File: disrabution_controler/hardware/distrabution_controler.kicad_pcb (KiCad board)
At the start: 4 copper layers, 246 x 110 mm, 266 parts, among them J1 Conn_Coaxial, J3 JTAG, J5 PROG_PORT, Q1 NMOS, Q10 PMOS, Q11 PMOS, Q12 PMOS, Q13 PMOS, Q14 PMOS, Q15 PMOS, Q16 PMOS, Q17 PMOS, Q18 PMOS, Q19 PMOS, Q2 NMOS, Q20 PMOS, Q3 NMOS, Q4 PMOS, Q5 PMOS, Q6 PMOS, Q7 PMOS, Q8 PMOS, Q9 PMOS, U1 TJA1043T/1J, U2 ESP32-S2FH2, U3 PI4IOE5V6416LEX, U4 ECMF02-2AMX6, U5 ADS7128, U6 ADS7128, U7 AP62150WU, Y1 40 MHz

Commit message: more hardware work on disrabution controler nearing ifc
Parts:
- added H20: MountingHole, MountingHole:MountingHole_4.3mm_M4, F.Cu at (49.4, 89.5)
- added H21: MountingHole, MountingHole:MountingHole_4.3mm_M4, F.Cu at (49.2, 124.5)
- added H22: MountingHole, MountingHole:MountingHole_4.3mm_M4, F.Cu at (189.3, 95.7)
- added H23: MountingHole, MountingHole:MountingHole_4.3mm_M4, F.Cu at (196.3, 129.1)
- added H24: MountingHole, MountingHole:MountingHole_4.3mm_M4, F.Cu at (250.1, 160.2)
- C1, C12, C13, C14, C15, C16, C17, C2, C3, C4, C5, C6, D20, D21, JP1, R1, R2, R21, R22, R32, R33: moved to B.Cu
- J2, U4: moved to F.Cu
- L1: footprint Resistor_SMD:R_0603_1608Metric -> Inductor_SMD:L_Bourns_SDR0604
- Q1, Q2, Q3: footprint Resistor_SMD:R_0603_1608Metric -> Package_TO_SOT_SMD:SOT-23
- moved TP25 314.0 mm to (210.8, 78.4)
- moved L1 312.4 mm to (208.8, 83.4), turned to 90 degrees
- moved TP29 311.3 mm to (207.0, 91.0), turned to 180 degrees
- moved C34 309.9 mm to (212.9, 87.2), turned to -90 degrees
- moved Q2 305.6 mm to (202.0, 89.3), turned to 180 degrees
- moved TP26 305.4 mm to (209.0, 91.0), turned to 180 degrees
- moved Q3 304.9 mm to (202.0, 92.7), turned to 180 degrees
- moved R53 303.5 mm to (207.5, 88.0), turned to 180 degrees
- moved C32 303.0 mm to (202.7, 83.0)
- moved TP2 302.7 mm to (248.3, 94.0)
- moved TP1 302.1 mm to (248.3, 91.9)
- moved R51 301.4 mm to (210.5, 88.0), turned to 180 degrees
- moved TP28 301.3 mm to (196.0, 92.2)
- moved C33 301.0 mm to (199.2, 85.5), turned to 90 degrees
- moved TP27 300.6 mm to (196.0, 90.1), turned to 90 degrees
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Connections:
- net Net-(J1-In) renamed LNA
- D20 pad 5: ESP_RX -> GPIO12
- D20 pad 6: unconnected-(D20-K5-Pad6) -> ESP_RX
- D20 pad 7: GPIO12 -> RST
- D20 pad 8: unconnected-(D20-K7-Pad8) -> ESP_IO0
- D21 pad 1: GPIO11 -> GPIO6
- D21 pad 2: GPIO10 -> GPIO8
- D21 pad 4: GPIO9 -> GPIO11
- D21 pad 5: GPIO8 -> DAC_2
- D21 pad 6: GPIO7 -> DAC_1
- D21 pad 7: GPIO6 -> GPIO10
- D21 pad 8: DAC_2 -> GPIO9
- D21 pad 9: DAC_1 -> GPIO7
- Q1 pad 1: CAR_ACC -> /MCU_IO/CAR_ACC_ESD
- Q1 pad 2: /MCU_IO/CAR_ACC_ESD -> GND
- Q2 pad 1: Net-(Q2-D) -> Net-(Q2-G)
- Q2 pad 2: Net-(Q2-G) -> GND
- Q3 pad 1: Net-(Q2-G) -> ALLOW_Q_DRAW
- Q3 pad 2: ALLOW_Q_DRAW -> GND
- U2 pad 37: CAN_WAKE -> CAN_ERR
- U2 pad 38: CAN_ERR -> CAN_WAKE
- U2 pad 40: CAN_EN -> CAN_TX
- U2 pad 42: CAN_TX -> CAN_EN
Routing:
- net +3V3: track 27.7 -> 679.7 mm, vias 4 -> 40
- net I2C_SDA: track 0.00 -> 327.9 mm, vias 0 -> 7
- net I2C_SCL: track 0.00 -> 327.2 mm, vias 0 -> 6
- net Net-(D16-DIN): track 0.00 -> 288.3 mm, vias 0 -> 2
- net RST: track 0.00 -> 245.0 mm, vias 0 -> 3
- net DISRABUTION_NEO_PIXELS: track 0.00 -> 232.2 mm, vias 0 -> 2
- net CAR_ACC: track 0.00 -> 198.8 mm
- net IOX0_INT: track 6.40 -> 181.3 mm, vias 0 -> 3
- net ADC_02_ALERT: track 0.00 -> 160.0 mm, vias 0 -> 4
- net ADC_01_ALERT: track 0.00 -> 134.2 mm, vias 0 -> 4
- net GPIO12: track 0.00 -> 124.1 mm, vias 0 -> 1
- net GPIO6: track 0.00 -> 103.9 mm
- net GPIO7: track 0.00 -> 96.2 mm
- net DAC_1: track 0.00 -> 92.4 mm, vias 0 -> 2
- net ESP_RX: track 0.00 -> 89.1 mm, vias 0 -> 1
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- added copper zone on B.Cu, net +3V3
- added copper zone on F.Cu, net +3V3
- added copper zone on F.Cu, net GND
- added copper zone on In2.Cu, net GND
- added copper zone on F.Cu, net Net-(U7-BST)
- added copper zone on In2.Cu, net PERIPHERAL_PWR
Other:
- board text added: "+3V3"
- board text added: "CAR POWER SYSTEM DISRABUTION CONTROLER REV A TOKYO ANDREANA GPL-3.0 FLA PER CHANEL SHAL NOT EXCEED 30A"
- board text added: "CHANEL 1"
- board text added: "CHANEL 10"
- board text added: "CHANEL 11"
- board text added: "CHANEL 12"
- board text added: "CHANEL 13"
- board text added: "CHANEL 14"
- board text added: "CHANEL 15"
- board text added: "CHANEL 16"
- board text added: "CHANEL 2"
- board text added: "CHANEL 3"
- board text added: "CHANEL 4"
- board text added: "CHANEL 5"
- board text added: "CHANEL 6"
- board text added: "CHANEL 7"
- board text added: "CHANEL 8"
- board text added: "CHANEL 9"
- board text added: "GND"
- board text added: "IO0"
- board text added: "JTAG"
- board text added: "MDT0"
- board text added: "MTCK"
- board text added: "MTDI"
- board text added: "MTMS"
- board text added: "PROG"
- board text added: "RST"
- board text added: "RX"
- board text added: "TX"
- board text added: "WI-FI"

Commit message: fixed haredware issue
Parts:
- added Q21: NMOS, Package_TO_SOT_SMD:SOT-23, F.Cu at (27.0, 132.0)
- added Q22: NMOS, Package_TO_SOT_SMD:SOT-23, F.Cu at (49.0, 132.0)
- added Q23: NMOS, Package_TO_SOT_SMD:SOT-23, F.Cu at (71.0, 132.0)
- added Q24: NMOS, Package_TO_SOT_SMD:SOT-23, F.Cu at (167.2, 113.5)
- added Q25: NMOS, Package_TO_SOT_SMD:SOT-23, F.Cu at (93.0, 132.0)
- added Q26: NMOS, Package_TO_SOT_SMD:SOT-23, F.Cu at (115.0, 132.0)
- added Q27: NMOS, Package_TO_SOT_SMD:SOT-23, F.Cu at (137.0, 132.0)
- added Q28: NMOS, Package_TO_SOT_SMD:SOT-23, F.Cu at (159.0, 132.0)
- added Q29: NMOS, Package_TO_SOT_SMD:SOT-23, F.Cu at (181.0, 132.0)
- added Q30: NMOS, Package_TO_SOT_SMD:SOT-23, F.Cu at (188.7, 86.0)
- added Q31: NMOS, Package_TO_SOT_SMD:SOT-23, F.Cu at (166.9, 86.0)
- added Q32: NMOS, Package_TO_SOT_SMD:SOT-23, F.Cu at (144.7, 86.0)
- added Q33: NMOS, Package_TO_SOT_SMD:SOT-23, F.Cu at (122.8, 86.0)
- added Q34: NMOS, Package_TO_SOT_SMD:SOT-23, F.Cu at (100.7, 86.0)
- added Q35: NMOS, Package_TO_SOT_SMD:SOT-23, F.Cu at (78.8, 86.0)
- added Q36: NMOS, Package_TO_SOT_SMD:SOT-23, F.Cu at (56.9, 86.0)
- added Q37: NMOS, Package_TO_SOT_SMD:SOT-23, F.Cu at (34.8, 86.0)
- added TP48: ~, TestPoint:TestPoint_Pad_D1.0mm, F.Cu at (24.0, 129.7)
- added TP49: ~, TestPoint:TestPoint_Pad_D1.0mm, F.Cu at (46.0, 129.7)
- added TP50: ~, TestPoint:TestPoint_Pad_D1.0mm, F.Cu at (68.0, 129.7)
- added TP51: ~, TestPoint:TestPoint_Pad_D1.0mm, F.Cu at (90.0, 129.7)
- added TP52: ~, TestPoint:TestPoint_Pad_D1.0mm, F.Cu at (112.0, 129.7)
- added TP53: ~, TestPoint:TestPoint_Pad_D1.0mm, F.Cu at (134.0, 129.7)
- added TP54: ~, TestPoint:TestPoint_Pad_D1.0mm, F.Cu at (156.0, 129.7)
- added TP55: ~, TestPoint:TestPoint_Pad_D1.0mm, F.Cu at (178.0, 129.7)
- added TP56: ~, TestPoint:TestPoint_Pad_D1.0mm, F.Cu at (191.3, 88.4)
- added TP57: ~, TestPoint:TestPoint_Pad_D1.0mm, F.Cu at (169.2, 88.6)
- added TP58: ~, TestPoint:TestPoint_Pad_D1.0mm, F.Cu at (147.2, 88.4)
- added TP59: ~, TestPoint:TestPoint_Pad_D1.0mm, F.Cu at (125.4, 88.4)
- added TP60: ~, TestPoint:TestPoint_Pad_D1.0mm, F.Cu at (103.3, 88.4)
- added TP61: ~, TestPoint:TestPoint_Pad_D1.0mm, F.Cu at (81.2, 88.7)
- added TP62: ~, TestPoint:TestPoint_Pad_D1.0mm, F.Cu at (59.4, 88.4)
- added TP63: ~, TestPoint:TestPoint_Pad_D1.0mm, F.Cu at (37.2, 88.5)
- added TP64: ~, TestPoint:TestPoint_Pad_D1.0mm, F.Cu at (168.4, 117.5)
- F1, F10, F11, F12, F13, F14, F15, F16, F17, F2, F3, F4, F5, F6, F7, F8, F9: value Fuse_Small -> ~
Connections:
- net IOX0_INT renamed IOX_0_INT
- Q10 pad 4: CH7_GATE -> Net-(Q10-G)
- Q11 pad 4: CH8_GATE -> Net-(Q11-G)
- Q12 pad 4: CH9_GATE -> Net-(Q12-G)
- Q13 pad 4: CH10_GATE -> Net-(Q13-G)
- Q14 pad 4: CH11_GATE -> Net-(Q14-G)
- Q15 pad 4: CH12_GATE -> Net-(Q15-G)
- Q16 pad 4: CH13_GATE -> Net-(Q16-G)
- Q17 pad 4: CH14_GATE -> Net-(Q17-G)
- Q18 pad 4: CH15_GATE -> Net-(Q18-G)
- Q19 pad 4: CH16_GATE -> Net-(Q19-G)
- Q20 pad 4: PERIPHERAL_PWR_GATE -> Net-(Q20-G)
- Q4 pad 4: CH1_GATE -> Net-(Q21-D)
- Q5 pad 4: CH2_GATE -> Net-(Q22-D)
- Q6 pad 4: CH3_GATE -> Net-(Q23-D)
- Q7 pad 4: CH4_GATE -> Net-(Q25-D)
- Q8 pad 4: CH5_GATE -> Net-(Q26-D)
- Q9 pad 4: CH6_GATE -> Net-(Q27-D)
- R56 pad 2: CH1_GATE -> Net-(Q21-D)
- R57 pad 2: CH2_GATE -> Net-(Q22-D)
- R58 pad 2: CH3_GATE -> Net-(Q23-D)
- R59 pad 2: CH4_GATE -> Net-(Q25-D)
- R60 pad 2: CH5_GATE -> Net-(Q26-D)
- R61 pad 2: CH6_GATE -> Net-(Q27-D)
- R62 pad 2: CH7_GATE -> Net-(Q10-G)
- R63 pad 2: CH8_GATE -> Net-(Q11-G)
- R72 pad 2: CH9_GATE -> Net-(Q12-G)
- R73 pad 2: CH10_GATE -> Net-(Q13-G)
- R74 pad 2: CH11_GATE -> Net-(Q14-G)
- R75 pad 2: CH12_GATE -> Net-(Q15-G)
- R76 pad 2: CH13_GATE -> Net-(Q16-G)
- R77 pad 2: CH14_GATE -> Net-(Q17-G)
- R78 pad 2: CH15_GATE -> Net-(Q18-G)
- R79 pad 2: CH16_GATE -> Net-(Q19-G)
- R88 pad 2: PERIPHERAL_PWR_GATE -> Net-(Q20-G)
- TP30 pad 1: CH1_GATE -> Net-(Q21-D)
- TP31 pad 1: CH2_GATE -> Net-(Q22-D)
- TP32 pad 1: CH3_GATE -> Net-(Q23-D)
- TP33 pad 1: CH4_GATE -> Net-(Q25-D)
- TP34 pad 1: CH5_GATE -> Net-(Q26-D)
- TP35 pad 1: CH6_GATE -> Net-(Q27-D)
- TP36 pad 1: CH7_GATE -> Net-(Q10-G)
- TP37 pad 1: CH8_GATE -> Net-(Q11-G)
- TP38 pad 1: CH9_GATE -> Net-(Q12-G)
- TP39 pad 1: CH10_GATE -> Net-(Q13-G)
- TP40 pad 1: CH11_GATE -> Net-(Q14-G)
- TP41 pad 1: CH12_GATE -> Net-(Q15-G)
- TP42 pad 1: CH13_GATE -> Net-(Q16-G)
- TP43 pad 1: CH14_GATE -> Net-(Q17-G)
- TP44 pad 1: CH15_GATE -> Net-(Q18-G)
- TP45 pad 1: CH16_GATE -> Net-(Q19-G)
- TP47 pad 1: PERIPHERAL_PWR_GATE -> Net-(Q20-G)
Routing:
- net GND: track 128.0 -> 145.9 mm, vias 71 -> 88
- net CH3_GATE: track 44.7 -> 29.5 mm, vias 2 -> 1
- net CH7_GATE: track 130.2 -> 115.1 mm, vias 2 -> 1
- net CH4_GATE: track 65.9 -> 50.9 mm, vias 2 -> 1
- net CH6_GATE: track 108.6 -> 93.7 mm, vias 2 -> 1
- net CH5_GATE: track 87.2 -> 72.3 mm, vias 2 -> 1
- net CH8_GATE: track 151.3 -> 136.5 mm, vias 2 -> 1
- net CH16_GATE: track 37.8 -> 23.4 mm, vias 2 -> 1
- net PERIPHERAL_PWR_GATE: track 75.4 -> 64.1 mm
- net Net-(Q19-G): track 0.00 -> 8.27 mm
- net Net-(Q12-G): track 0.00 -> 7.32 mm
- net Net-(Q20-G): track 0.00 -> 7.21 mm
- net Net-(Q10-G): track 0.00 -> 6.73 mm
- net Net-(Q11-G): track 0.00 -> 6.73 mm
- net Net-(Q22-D): track 0.00 -> 6.73 mm
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
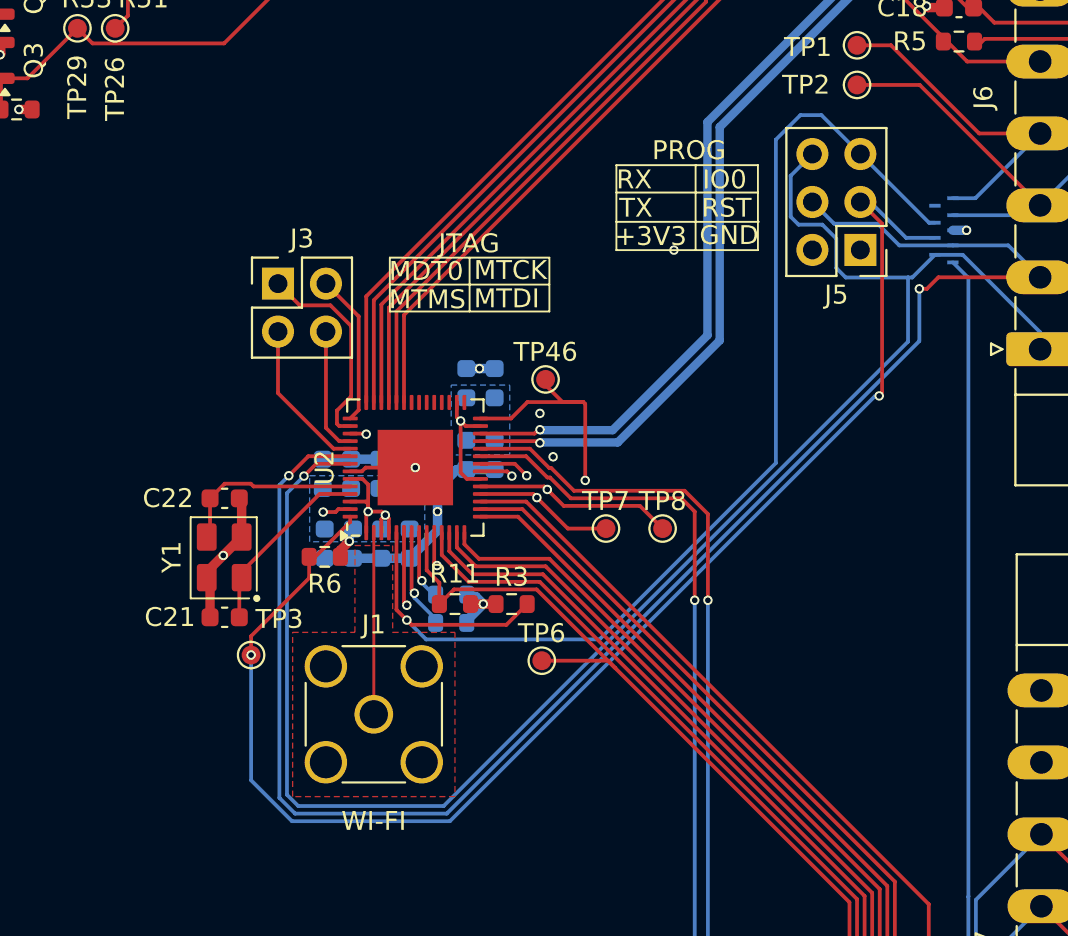
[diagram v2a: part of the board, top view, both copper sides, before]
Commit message: changed programing headder
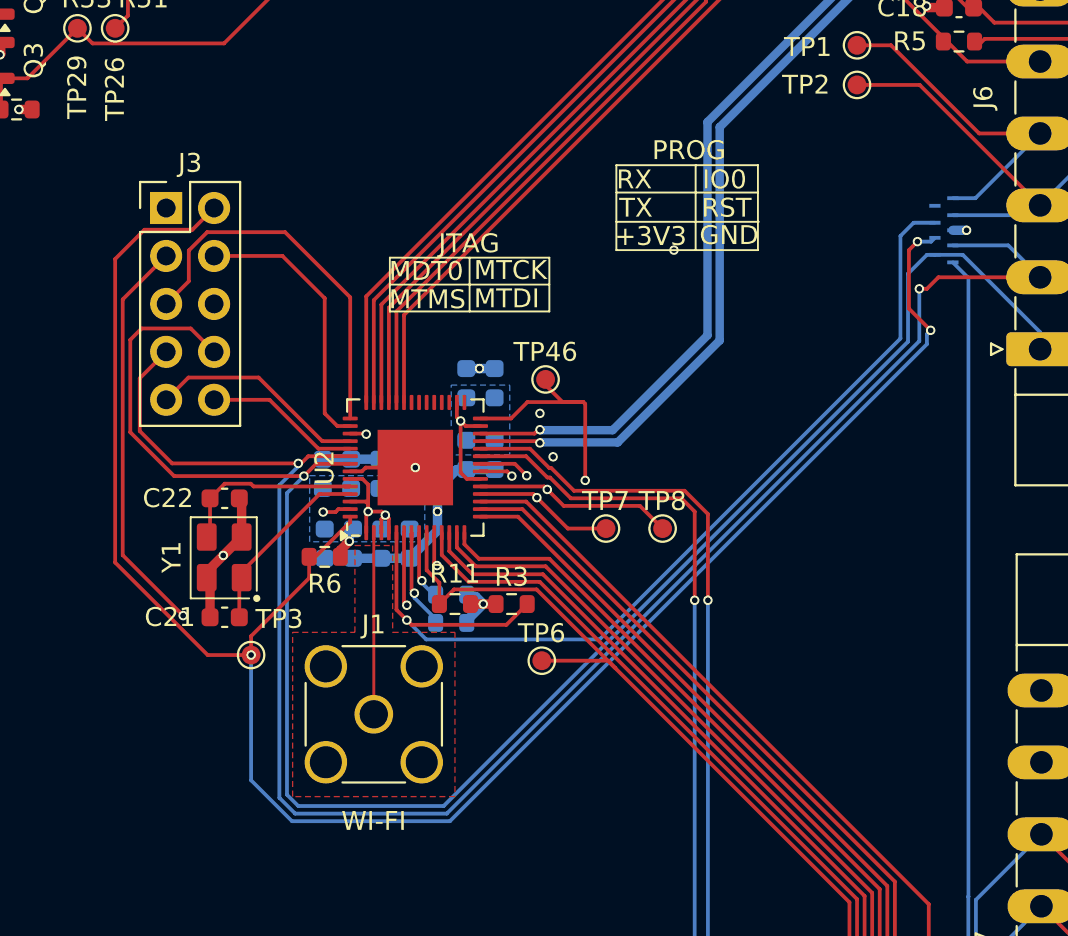
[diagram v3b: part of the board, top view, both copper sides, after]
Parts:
- removed J5: PROG_PORT, Connector_PinHeader_2.54mm:PinHeader_2x03_P2.54mm_Vertical
- J3: value JTAG -> ~; footprint Connector_PinHeader_2.54mm:PinHeader_2x02_P2.54mm_Vertical -> Connector_PinHeader_2.54mm:PinHeader_2x05_P2.54mm_Vertical
- R24, R25, R26, R27, R28, R29, R30, R31, R32, R33, R43, R44, R45, R46, R47, R48, R49, R50: value 20K -> 2K
- moved J3 7.15 mm to (211.7, 100.5)
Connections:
- J3 pad 1: MTD0 -> GND
- J3 pad 2: MTCK -> RST
- J3 pad 3: MTMS -> ESP_IO0
- J3 pad 4: MTDI -> MTD0
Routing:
- net RST: track 245.0 -> 271.9 mm, vias 3 -> 4
- net ESP_IO0: track 64.1 -> 85.8 mm, vias 1 -> 2
- net MTCK: track 8.05 -> 20.1 mm
- net ESP_RX: track 89.1 -> 97.2 mm
- net +3V3: track 679.7 -> 672.3 mm
- net ESP_TX: track 88.7 -> 94.3 mm
- net MTDI: track 6.68 -> 11.6 mm
- net MTD0: track 11.0 -> 14.5 mm
- net ADC_02_ALERT: track 160.0 -> 160.8 mm
